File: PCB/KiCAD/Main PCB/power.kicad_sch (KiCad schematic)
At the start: 6 parts, among them J8 Conn_01x02, J9 Conn_01x02

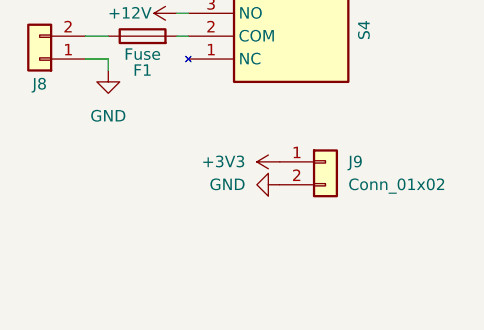
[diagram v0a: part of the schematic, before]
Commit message: Added kicker and spare serial and i2c
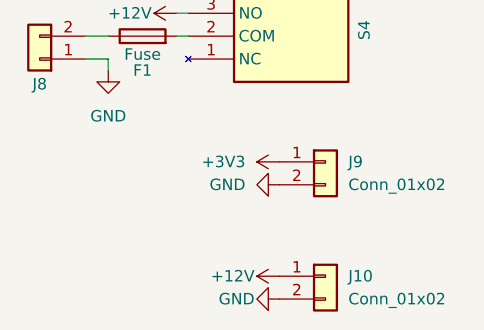
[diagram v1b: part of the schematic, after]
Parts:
- added J10: Conn_01x02, Connector_AMASS:AMASS_XT30U-M_1x02_P5.0mm_Vertical, symbol Connector_Generic:Conn_01x02
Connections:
- net +12V: now also J10.1 (Pin_1)
- net GND: now also J10.2 (Pin_2)
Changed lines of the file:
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@@
+	(symbol
+		(lib_id "power:GND")
+		(at 148.59 142.24 270)
+		(unit 1)
+		(exclude_from_sim no)
+		(in_bom yes)
+		(on_board yes)
+		(dnp no)
+		(property "Reference" "#PWR0136"
+			(at 142.24 142.24 0)
+			(effects
+				(font
+					(size 1.27 1.27)
+				)
+				(hide yes)
+			)
+		)
+		(property "Value" "GND"
+			(at 145.796 142.24 90)
+			(effects
+				(font
+					(size 1.27 1.27)
+				)
+				(justify right)
+			)
+		)
+		(property "Footprint" ""
+			(at 148.59 142.24 0)
+			(effects
+				(font
+					(size 1.27 1.27)
+				)
+				(hide yes)
+			)
+		)
+		(property "Datasheet" ""
+			(at 148.59 142.24 0)
+			(effects
+				(font
+					(size 1.27 1.27)
+				)
+				(hide yes)
+			)
+		)
+		(property "Description" "Power symbol creates a global label with name \"GND\" , ground"
+			(at 148.59 142.24 0)
+			(effects
+				(font
+					(size 1.27 1.27)
+				)
+				(hide yes)
+			)
+		)
+		(pin "1"
+		)
+		(instances
+			(project "Main PCB"
+				(path "/2fa7e914-8c49-49b7-a5a9-3cb78b2e953f/32920b8a-8ee4-4be3-8c67-c1587aa84161"
+					(reference "#PWR0136")
+					(unit 1)
+				)
+			)
+		)
+	)
 	(symbol
 		(lib_id "power:GND")
@@
 	(symbol
 		(lib_id "Connector_Generic:Conn_01x02")
+		(at 153.67 139.7 0)
+		(unit 1)
+		(exclude_from_sim no)
+		(in_bom yes)
+		(on_board yes)
+		(dnp no)
+		(fields_autoplaced yes)
+		(property "Reference" "J10"
+			(at 156.21 139.6999 0)
+			(effects
+				(font
+					(size 1.27 1.27)
+				)
+				(justify left)
+			)
+		)
+		(property "Value" "Conn_01x02"
+			(at 156.21 142.2399 0)
+			(effects
+				(font
+					(size 1.27 1.27)
+				)
+				(justify left)
+			)
+		)
+		(property "Footprint" "Connector_AMASS:AMASS_XT30U-M_1x02_P5.0mm_Vertical"
+			(at 153.67 139.7 0)
+			(effects
+				(font
+					(size 1.27 1.27)
+				)
+				(hide yes)
+			)
+		)
+		(property "Datasheet" "~"
+			(at 153.67 139.7 0)
+			(effects
+				(font
+					(size 1.27 1.27)
+				)
+				(hide yes)
+			)
+		)
+		(property "Description" "Generic connector, single row, 01x02, script generated (kicad-library-utils/schlib/autogen/connector/)"
+			(at 153.67 139.7 0)
+			(effects
+				(font
+					(size 1.27 1.27)
+				)
+				(hide yes)
+			)
+		)
+		(pin "1"
+		)
+		(pin "2"
+		)
+		(instances
+			(project ""
+				(path "/2fa7e914-8c49-49b7-a5a9-3cb78b2e953f/32920b8a-8ee4-4be3-8c67-c1587aa84161"
+					(reference "J10")
+					(unit 1)
+				)
+			)
+		)
+	)
+	(symbol
+		(lib_id "Connector_Generic:Conn_01x02")
 		(at 121.92 115.57 180)
 		(unit 1)
@@
 					(unit 1)
 				)
+			)
+		)
+	)
+	(symbol
+		(lib_id "power:+12V")
+		(at 148.59 139.7 90)
+		(unit 1)
+		(exclude_from_sim no)
+		(in_bom yes)
+		(on_board yes)
+		(dnp no)
+		(property "Reference" "#PWR0135"
+			(at 152.4 139.7 0)
+			(effects
+				(font
+					(size 1.27 1.27)
+				)
+				(hide yes)
+			)
+		)
+		(property "Value" "+12V"
+			(at 145.796 139.7 90)
+			(effects
+				(font
+					(size 1.27 1.27)
+				)
+				(justify left)
+			)
+		)
+		(property "Footprint" ""
+			(at 148.59 139.7 0)
+			(effects
+				(font
+					(size 1.27 1.27)
+				)
+				(hide yes)
+			)
+		)
+		(property "Datasheet" ""
+			(at 148.59 139.7 0)
+			(effects
+				(font
+					(size 1.27 1.27)
+				)
+				(hide yes)
+			)
+		)
+		(property "Description" "Power symbol creates a global label with name \"+12V\""
+			(at 148.59 139.7 0)
+			(effects
+				(font
+					(size 1.27 1.27)
+				)
+				(hide yes)
+			)
+		)
+		(pin "1"
+		)
+		(instances
+			(project "Main PCB"
+				(path "/2fa7e914-8c49-49b7-a5a9-3cb78b2e953f/32920b8a-8ee4-4be3-8c67-c1587aa84161"
+					(reference "#PWR0135")
+					(unit 1)
+				)

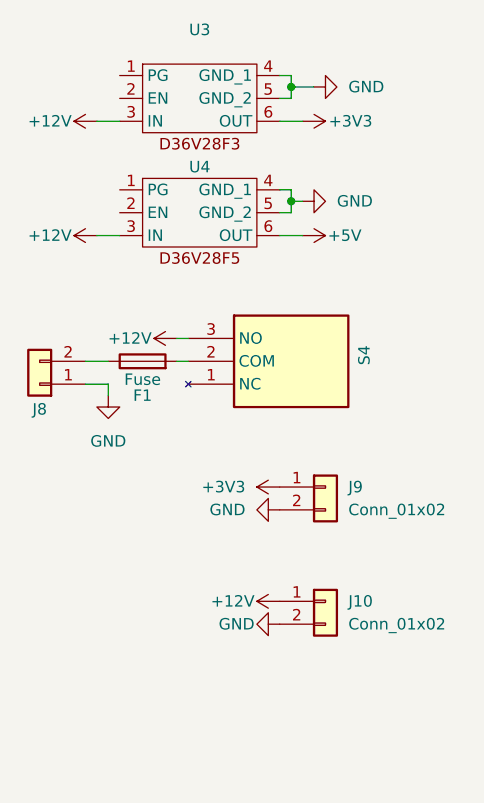
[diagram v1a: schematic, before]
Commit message: Added a BNO055 and traced PCB (incomplete, no DRC pass)
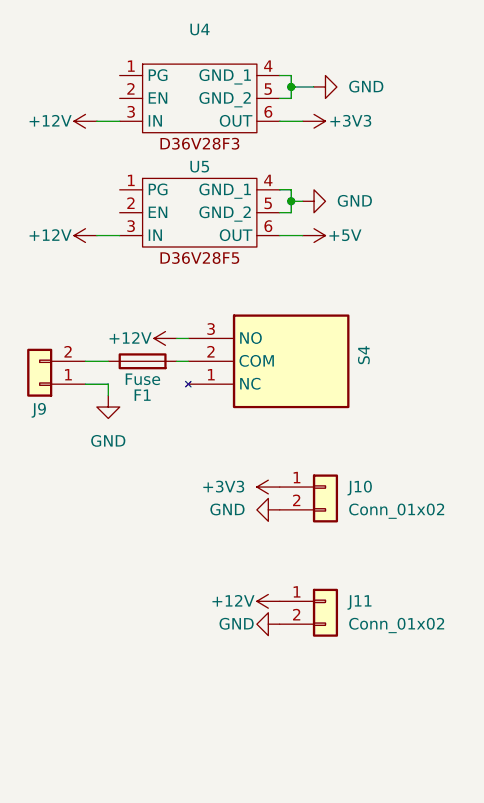
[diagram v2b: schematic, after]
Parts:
- renumbered J9 to J10, J10 to J11, J8 to J9, U3 to U4, U4 to U5
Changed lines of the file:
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@@
 		(dnp no)
 		(fields_autoplaced yes)
-		(property "Reference" "U3"
+		(property "Reference" "U4"
 			(at 139.7 76.2 0)
 			(effects
@@
 			(project ""
 				(path "/2fa7e914-8c49-49b7-a5a9-3cb78b2e953f/32920b8a-8ee4-4be3-8c67-c1587aa84161"
-					(reference "U3")
+					(reference "U4")
 					(unit 1)
 				)
@@
 		(dnp no)
 		(fields_autoplaced yes)
-		(property "Reference" "#PWR0129"
+		(property "Reference" "#PWR0133"
 			(at 152.4 127 0)
 			(effects
@@
 			(project "Main PCB"
 				(path "/2fa7e914-8c49-49b7-a5a9-3cb78b2e953f/32920b8a-8ee4-4be3-8c67-c1587aa84161"
-					(reference "#PWR0129")
+					(reference "#PWR0133")
 					(unit 1)
 				)
@@
 		(dnp no)
 		(fields_autoplaced yes)
-		(property "Reference" "#PWR0127"
+		(property "Reference" "#PWR0131"
 			(at 129.54 123.19 0)
 			(effects
@@
 			(project "Main PCB"
 				(path "/2fa7e914-8c49-49b7-a5a9-3cb78b2e953f/32920b8a-8ee4-4be3-8c67-c1587aa84161"
-					(reference "#PWR0127")
+					(reference "#PWR0131")
 					(unit 1)
 				)
@@
 		(on_board yes)
 		(dnp no)
-		(property "Reference" "#PWR0126"
+		(property "Reference" "#PWR0130"
 			(at 132.08 99.06 0)
 			(effects
@@
 			(project "Main PCB"
 				(path "/2fa7e914-8c49-49b7-a5a9-3cb78b2e953f/32920b8a-8ee4-4be3-8c67-c1587aa84161"
-					(reference "#PWR0126")
+					(reference "#PWR0130")
 					(unit 1)
 				)
@@
 		(dnp no)
 		(fields_autoplaced yes)
-		(property "Reference" "J9"
+		(property "Reference" "J10"
 			(at 156.21 126.9999 0)
 			(effects
@@
 			(project "Main PCB"
 				(path "/2fa7e914-8c49-49b7-a5a9-3cb78b2e953f/32920b8a-8ee4-4be3-8c67-c1587aa84161"
-					(reference "J9")
+					(reference "J10")
 					(unit 1)
 				)
@@
 		(on_board yes)
 		(dnp no)
-		(property "Reference" "#PWR0133"
+		(property "Reference" "#PWR0139"
 			(at 147.32 99.06 0)
 			(effects
@@
 			(project "Main PCB"
 				(path "/2fa7e914-8c49-49b7-a5a9-3cb78b2e953f/32920b8a-8ee4-4be3-8c67-c1587aa84161"
-					(reference "#PWR0133")
+					(reference "#PWR0139")
 					(unit 1)
 				)
@@
 		(on_board yes)
 		(dnp no)
-		(property "Reference" "#PWR0131"
+		(property "Reference" "#PWR0137"
 			(at 147.32 86.36 0)
 			(effects
@@
 			(project "Main PCB"
 				(path "/2fa7e914-8c49-49b7-a5a9-3cb78b2e953f/32920b8a-8ee4-4be3-8c67-c1587aa84161"
-					(reference "#PWR0131")
+					(reference "#PWR0137")
 					(unit 1)
 				)
@@
 		(on_board yes)
 		(dnp no)
-		(property "Reference" "U4"
+		(property "Reference" "U5"
 			(at 139.7 91.44 0)
 			(effects
@@
 			(project "Main PCB"
 				(path "/2fa7e914-8c49-49b7-a5a9-3cb78b2e953f/32920b8a-8ee4-4be3-8c67-c1587aa84161"
-					(reference "U4")
+					(reference "U5")
 					(unit 1)
 				)
@@
 		(dnp no)
 		(fields_autoplaced yes)
-		(property "Reference" "#PWR0134"
+		(property "Reference" "#PWR0140"
 			(at 158.75 82.55 0)
 			(effects
@@
 			(project "Main PCB"
 				(path "/2fa7e914-8c49-49b7-a5a9-3cb78b2e953f/32920b8a-8ee4-4be3-8c67-c1587aa84161"
-					(reference "#PWR0134")
+					(reference "#PWR0140")
 					(unit 1)
 				)
@@
 		(dnp no)
 		(fields_autoplaced yes)
-		(property "Reference" "#PWR0130"
+		(property "Reference" "#PWR0134"
 			(at 142.24 129.54 0)
 			(effects
@@
 			(project "Main PCB"
 				(path "/2fa7e914-8c49-49b7-a5a9-3cb78b2e953f/32920b8a-8ee4-4be3-8c67-c1587aa84161"
-					(reference "#PWR0130")
+					(reference "#PWR0134")
 					(unit 1)
 				)
@@
 		(dnp no)
 		(fields_autoplaced yes)
-		(property "Reference" "J10"
+		(property "Reference" "J11"
 			(at 156.21 139.6999 0)
 			(effects
@@
 			(project ""
 				(path "/2fa7e914-8c49-49b7-a5a9-3cb78b2e953f/32920b8a-8ee4-4be3-8c67-c1587aa84161"
-					(reference "J10")
+					(reference "J11")
 					(unit 1)
 				)
@@
 		(on_board yes)
 		(dnp no)
-		(property "Reference" "J8"
+		(property "Reference" "J9"
 			(at 121.92 118.364 0)
 			(effects
@@
 			(project "Main PCB"
 				(path "/2fa7e914-8c49-49b7-a5a9-3cb78b2e953f/32920b8a-8ee4-4be3-8c67-c1587aa84161"
-					(reference "J8")
+					(reference "J9")
 					(unit 1)
 				)
@@
 		(on_board yes)
 		(dnp no)
-		(property "Reference" "#PWR0125"
+		(property "Reference" "#PWR0129"
 			(at 132.08 86.36 0)
 			(effects
@@
 			(project "Main PCB"
 				(path "/2fa7e914-8c49-49b7-a5a9-3cb78b2e953f/32920b8a-8ee4-4be3-8c67-c1587aa84161"
-					(reference "#PWR0125")
+					(reference "#PWR0129")
 					(unit 1)
 				)
@@
 		(on_board yes)
 		(dnp no)
-		(property "Reference" "#PWR0128"
+		(property "Reference" "#PWR0132"
 			(at 140.97 110.49 0)
 			(effects
@@
 			(project "Main PCB"
 				(path "/2fa7e914-8c49-49b7-a5a9-3cb78b2e953f/32920b8a-8ee4-4be3-8c67-c1587aa84161"
-					(reference "#PWR0128")
+					(reference "#PWR0132")
 					(unit 1)
 				)
@@
 		(dnp no)
 		(fields_autoplaced yes)
-		(property "Reference" "#PWR0132"
+		(property "Reference" "#PWR0138"
 			(at 157.48 95.25 0)
 			(effects
@@
 			(project "Main PCB"
 				(path "/2fa7e914-8c49-49b7-a5a9-3cb78b2e953f/32920b8a-8ee4-4be3-8c67-c1587aa84161"
-					(reference "#PWR0132")
-					(unit 1)
-				)
+					(reference "#PWR0138")
+					(unit 1)
+				)

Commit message: Added another switch
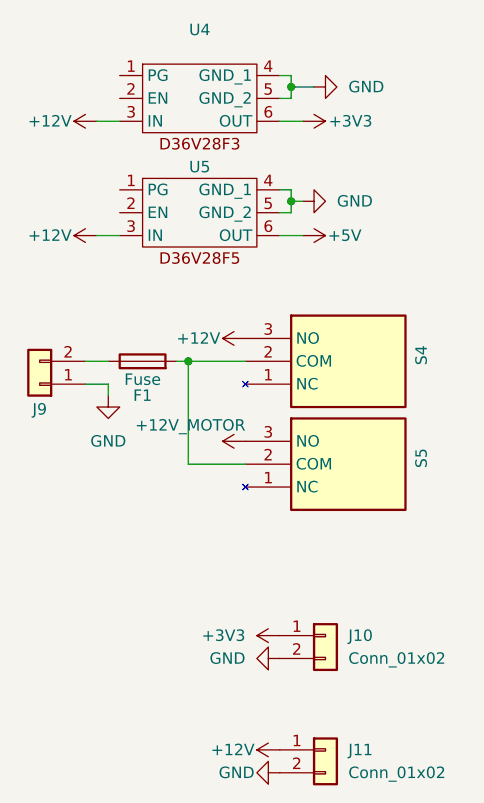
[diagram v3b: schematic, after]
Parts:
- added S5: 1101M2S3CGE2, 1101M2S3CGE2:1101M2S3CGE2, symbol 1101M2S3CGE2:1101M2S3CGE2
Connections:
- net at F1.2, S4.2 (COM): now also S5.2 (COM)
- new net +12V_MOTOR: S5.3 (NO)
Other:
- moved on the sheet: J10, J11, S4
